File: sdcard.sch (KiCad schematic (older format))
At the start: 7 parts, among them J21 Micro_SD_Card_Det_Hirose_DM3AT

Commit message: Some small adjustments
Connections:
- net SS_SD renamed SS
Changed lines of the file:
@@
 $Descr A4 11693 8268
 encoding utf-8
-Sheet 12 12
+Sheet 11 12
 Title ""
 Date ""
@@
 SCK
 Text HLabel 3450 2850 0    50   Input ~ 0
-SS_SD
+SS
 $Comp
 L Device:R R?

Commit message: Complete functional design
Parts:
- renumbered C114 to C109, J21 to J10, R120 to R112, R121 to R113, R122 to R114, R123 to R115, R124 to R116
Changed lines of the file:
@@
 $EndDescr
 $Comp
-L Connector:Micro_SD_Card_Det_Hirose_DM3AT J21
+L Connector:Micro_SD_Card_Det_Hirose_DM3AT J10
 U 1 1 5BC78F11
 P 6000 3150
-F 0 "J21" H 5950 3967 50  0000 C CNN
+F 0 "J10" H 5950 3967 50  0000 C CNN
 F 1 "Micro_SD_Card_Det_Hirose_DM3AT" H 5950 3876 50  0000 C CNN
 F 2 "Connector_Card:microSD_HC_Hirose_DM3D-SF" H 8050 3850 50  0001 C CNN
@@
 AR Path="/5BC77F8A/5BC83407" Ref="R?"  Part="1"
 AR Path="/5BC77F8D/5BC83407" Ref="R?"  Part="1"
-AR Path="/5BC78E83/5BC83407" Ref="R124"  Part="1"
-F 0 "R124" H 4700 2450 50  0000 C CNN
+AR Path="/5BC78E83/5BC83407" Ref="R116"  Part="1"
+F 0 "R116" H 4700 2450 50  0000 C CNN
 F 1 "47k" H 4700 2550 50  0000 C CNN
 F 2 "Resistor_SMD:R_0603_1608Metric" V 4780 2500 50  0001 C CNN
@@
 SD_DETECT
 $Comp
-L power:GND #PWR0124
+L power:GND #PWR0108
 U 1 1 5BC834C8
 P 3450 3250
-F 0 "#PWR0124" H 3450 3000 50  0001 C CNN
+F 0 "#PWR0108" H 3450 3000 50  0001 C CNN
 F 1 "GND" V 3455 3122 50  0000 R CNN
 F 2 "" H 3450 3250 50  0001 C CNN
@@
 AR Path="/5BC77F8A/5BC8393A" Ref="R?"  Part="1"
 AR Path="/5BC77F8D/5BC8393A" Ref="R?"  Part="1"
-AR Path="/5BC78E83/5BC8393A" Ref="R123"  Part="1"
-F 0 "R123" H 4400 2450 50  0000 C CNN
+AR Path="/5BC78E83/5BC8393A" Ref="R115"  Part="1"
+F 0 "R115" H 4400 2450 50  0000 C CNN
 F 1 "47k" H 4400 2550 50  0000 C CNN
 F 2 "Resistor_SMD:R_0603_1608Metric" V 4480 2500 50  0001 C CNN
@@
 AR Path="/5BC77F8A/5BC842EF" Ref="R?"  Part="1"
 AR Path="/5BC77F8D/5BC842EF" Ref="R?"  Part="1"
-AR Path="/5BC78E83/5BC842EF" Ref="R122"  Part="1"
-F 0 "R122" H 4100 2450 50  0000 C CNN
+AR Path="/5BC78E83/5BC842EF" Ref="R114"  Part="1"
+F 0 "R114" H 4100 2450 50  0000 C CNN
 F 1 "47k" H 4100 2550 50  0000 C CNN
 F 2 "Resistor_SMD:R_0603_1608Metric" V 4180 2500 50  0001 C CNN
@@
 AR Path="/5BC77F8A/5BC84424" Ref="R?"  Part="1"
 AR Path="/5BC77F8D/5BC84424" Ref="R?"  Part="1"
-AR Path="/5BC78E83/5BC84424" Ref="R121"  Part="1"
-F 0 "R121" H 3800 2450 50  0000 C CNN
+AR Path="/5BC78E83/5BC84424" Ref="R113"  Part="1"
+F 0 "R113" H 3800 2450 50  0000 C CNN
 F 1 "47k" H 3800 2550 50  0000 C CNN
 F 2 "Resistor_SMD:R_0603_1608Metric" V 3880 2500 50  0001 C CNN
@@
 AR Path="/5BC77F8A/5BC8859F" Ref="R?"  Part="1"
 AR Path="/5BC77F8D/5BC8859F" Ref="R?"  Part="1"
-AR Path="/5BC78E83/5BC8859F" Ref="R120"  Part="1"
-F 0 "R120" H 3500 2450 50  0000 C CNN
+AR Path="/5BC78E83/5BC8859F" Ref="R112"  Part="1"
+F 0 "R112" H 3500 2450 50  0000 C CNN
 F 1 "47k" H 3500 2550 50  0000 C CNN
 F 2 "Resistor_SMD:R_0603_1608Metric" V 3580 2500 50  0001 C CNN
@@
 	3650 3450 5100 3450
 $Comp
-L power:GND #PWR0126
+L power:GND #PWR0110
 U 1 1 5BC89EBA
 P 6800 3650
-F 0 "#PWR0126" H 6800 3400 50  0001 C CNN
+F 0 "#PWR0110" H 6800 3400 50  0001 C CNN
 F 1 "GND" H 6805 3477 50  0000 C CNN
 F 2 "" H 6800 3650 50  0001 C CNN
@@
 P 4400 3850
 AR Path="/5BC54251/5BC90131" Ref="C?"  Part="1"
-AR Path="/5BC78E83/5BC90131" Ref="C114"  Part="1"
-F 0 "C114" H 4515 3896 50  0000 L CNN
+AR Path="/5BC78E83/5BC90131" Ref="C109"  Part="1"
+F 0 "C109" H 4515 3896 50  0000 L CNN
 F 1 "10uF" H 4515 3805 50  0000 L CNN
 F 2 "Capacitor_SMD:C_1206_3216Metric" H 4438 3700 50  0001 C CNN
@@
 VDD3V3
 $Comp
-L power:GND #PWR0125
+L power:GND #PWR0109
 U 1 1 5BC911BE
 P 4400 4000
-F 0 "#PWR0125" H 4400 3750 50  0001 C CNN
+F 0 "#PWR0109" H 4400 3750 50  0001 C CNN
 F 1 "GND" H 4405 3827 50  0000 C CNN
 F 2 "" H 4400 4000 50  0001 C CNN

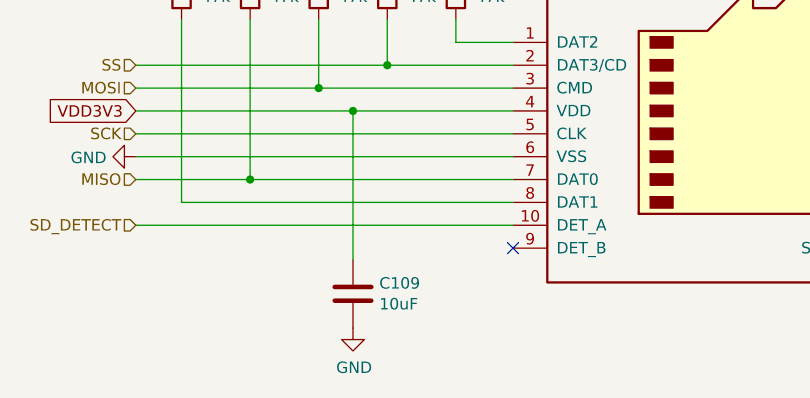
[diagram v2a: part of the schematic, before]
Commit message: Add bypass cap for I2C EEPROMs and redone some copper pour
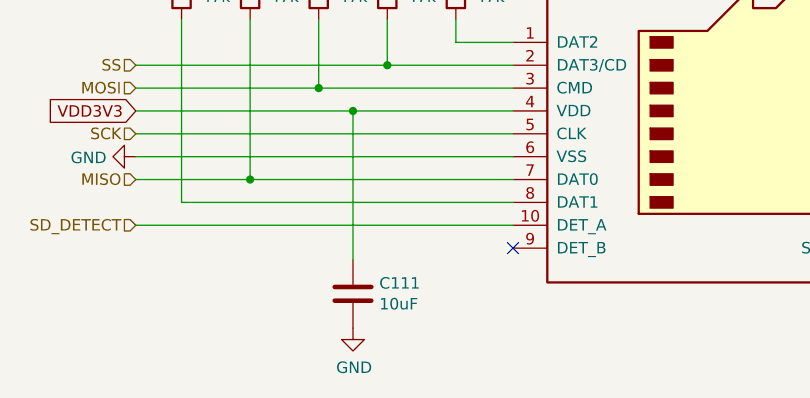
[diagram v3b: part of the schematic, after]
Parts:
- renumbered C109 to C111
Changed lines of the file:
@@
 SD_DETECT
 $Comp
-L power:GND #PWR0108
+L power:GND #PWR0110
 U 1 1 5BC834C8
 P 3450 3250
-F 0 "#PWR0108" H 3450 3000 50  0001 C CNN
+F 0 "#PWR0110" H 3450 3000 50  0001 C CNN
 F 1 "GND" V 3455 3122 50  0000 R CNN
 F 2 "" H 3450 3250 50  0001 C CNN
@@
 	3650 3450 5100 3450
 $Comp
-L power:GND #PWR0110
+L power:GND #PWR0112
 U 1 1 5BC89EBA
 P 6800 3650
-F 0 "#PWR0110" H 6800 3400 50  0001 C CNN
+F 0 "#PWR0112" H 6800 3400 50  0001 C CNN
 F 1 "GND" H 6805 3477 50  0000 C CNN
 F 2 "" H 6800 3650 50  0001 C CNN
@@
 P 4400 3850
 AR Path="/5BC54251/5BC90131" Ref="C?"  Part="1"
-AR Path="/5BC78E83/5BC90131" Ref="C109"  Part="1"
-F 0 "C109" H 4515 3896 50  0000 L CNN
+AR Path="/5BC78E83/5BC90131" Ref="C111"  Part="1"
+F 0 "C111" H 4515 3896 50  0000 L CNN
 F 1 "10uF" H 4515 3805 50  0000 L CNN
 F 2 "Capacitor_SMD:C_1206_3216Metric" H 4438 3700 50  0001 C CNN
@@
 VDD3V3
 $Comp
-L power:GND #PWR0109
+L power:GND #PWR0111
 U 1 1 5BC911BE
 P 4400 4000
-F 0 "#PWR0109" H 4400 3750 50  0001 C CNN
+F 0 "#PWR0111" H 4400 3750 50  0001 C CNN
 F 1 "GND" H 4405 3827 50  0000 C CNN
 F 2 "" H 4400 4000 50  0001 C CNN

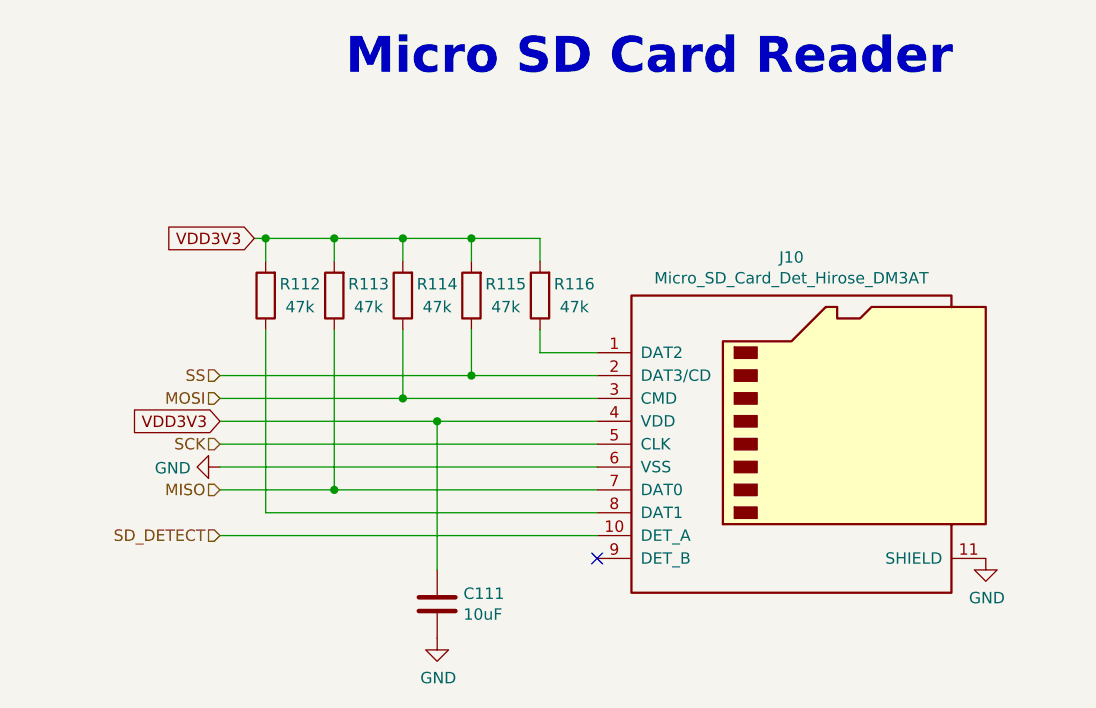
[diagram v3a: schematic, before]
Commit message: Add transistor for boot selection
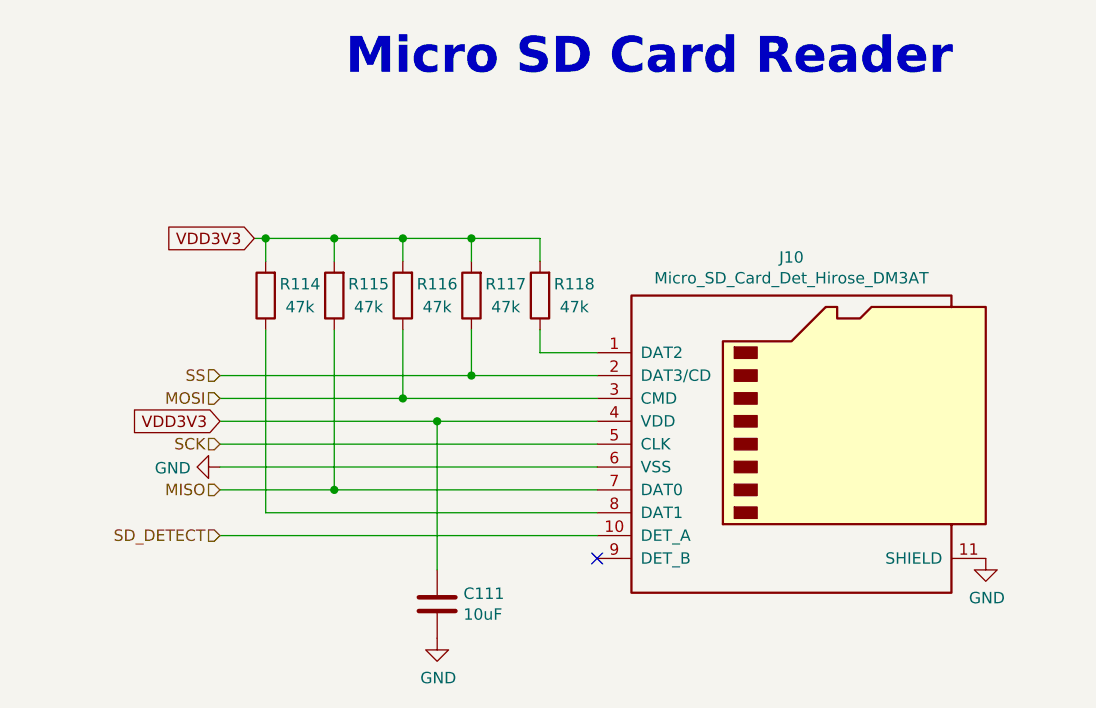
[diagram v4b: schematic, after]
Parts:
- renumbered R112 to R114, R113 to R115, R114 to R116, R115 to R117, R116 to R118
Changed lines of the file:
@@
 AR Path="/5BC77F8A/5BC83407" Ref="R?"  Part="1"
 AR Path="/5BC77F8D/5BC83407" Ref="R?"  Part="1"
-AR Path="/5BC78E83/5BC83407" Ref="R116"  Part="1"
-F 0 "R116" H 4700 2450 50  0000 C CNN
+AR Path="/5BC78E83/5BC83407" Ref="R118"  Part="1"
+F 0 "R118" H 4700 2450 50  0000 C CNN
 F 1 "47k" H 4700 2550 50  0000 C CNN
 F 2 "Resistor_SMD:R_0603_1608Metric" V 4780 2500 50  0001 C CNN
@@
 AR Path="/5BC77F8A/5BC8393A" Ref="R?"  Part="1"
 AR Path="/5BC77F8D/5BC8393A" Ref="R?"  Part="1"
-AR Path="/5BC78E83/5BC8393A" Ref="R115"  Part="1"
-F 0 "R115" H 4400 2450 50  0000 C CNN
+AR Path="/5BC78E83/5BC8393A" Ref="R117"  Part="1"
+F 0 "R117" H 4400 2450 50  0000 C CNN
 F 1 "47k" H 4400 2550 50  0000 C CNN
 F 2 "Resistor_SMD:R_0603_1608Metric" V 4480 2500 50  0001 C CNN
@@
 AR Path="/5BC77F8A/5BC842EF" Ref="R?"  Part="1"
 AR Path="/5BC77F8D/5BC842EF" Ref="R?"  Part="1"
-AR Path="/5BC78E83/5BC842EF" Ref="R114"  Part="1"
-F 0 "R114" H 4100 2450 50  0000 C CNN
+AR Path="/5BC78E83/5BC842EF" Ref="R116"  Part="1"
+F 0 "R116" H 4100 2450 50  0000 C CNN
 F 1 "47k" H 4100 2550 50  0000 C CNN
 F 2 "Resistor_SMD:R_0603_1608Metric" V 4180 2500 50  0001 C CNN
@@
 AR Path="/5BC77F8A/5BC84424" Ref="R?"  Part="1"
 AR Path="/5BC77F8D/5BC84424" Ref="R?"  Part="1"
-AR Path="/5BC78E83/5BC84424" Ref="R113"  Part="1"
-F 0 "R113" H 3800 2450 50  0000 C CNN
+AR Path="/5BC78E83/5BC84424" Ref="R115"  Part="1"
+F 0 "R115" H 3800 2450 50  0000 C CNN
 F 1 "47k" H 3800 2550 50  0000 C CNN
 F 2 "Resistor_SMD:R_0603_1608Metric" V 3880 2500 50  0001 C CNN
@@
 AR Path="/5BC77F8A/5BC8859F" Ref="R?"  Part="1"
 AR Path="/5BC77F8D/5BC8859F" Ref="R?"  Part="1"
-AR Path="/5BC78E83/5BC8859F" Ref="R112"  Part="1"
-F 0 "R112" H 3500 2450 50  0000 C CNN
+AR Path="/5BC78E83/5BC8859F" Ref="R114"  Part="1"
+F 0 "R114" H 3500 2450 50  0000 C CNN
 F 1 "47k" H 3500 2550 50  0000 C CNN
 F 2 "Resistor_SMD:R_0603_1608Metric" V 3580 2500 50  0001 C CNN

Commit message: Correct the name of the micro SD card reader
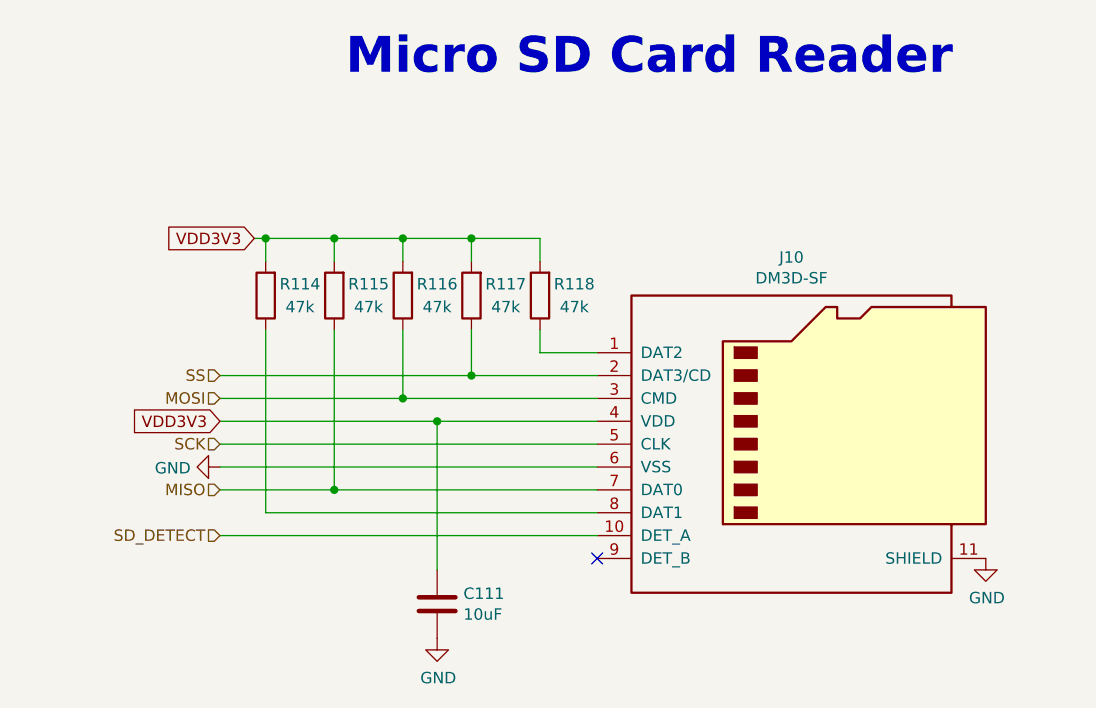
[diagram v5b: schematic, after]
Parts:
- J10: value Micro_SD_Card_Det_Hirose_DM3AT -> DM3D-SF
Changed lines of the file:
@@
 P 6000 3150
 F 0 "J10" H 5950 3967 50  0000 C CNN
-F 1 "Micro_SD_Card_Det_Hirose_DM3AT" H 5950 3876 50  0000 C CNN
+F 1 "DM3D-SF" H 5950 3876 50  0000 C CNN
 F 2 "Connector_Card:microSD_HC_Hirose_DM3D-SF" H 8050 3850 50  0001 C CNN
 F 3 "https://www.hirose.com/product/en/download_file/key_name/DM3/category/Catalog/doc_file_id/49662/?file_category_id=4&item_id=195&is_series=1" H 6000 3250 50  0001 C CNN

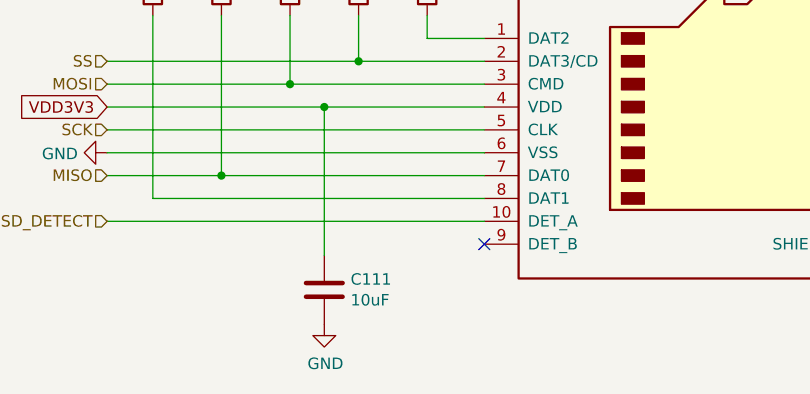
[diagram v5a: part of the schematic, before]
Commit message: Fix various v1.0 errors
 * Change 3.3V LDO to AP7365-33WG-7
 * Optimize soldermask clearance (from 0.2 to 0.05)
 * Connect SD connect switch to GND
 * Optimized some PADs
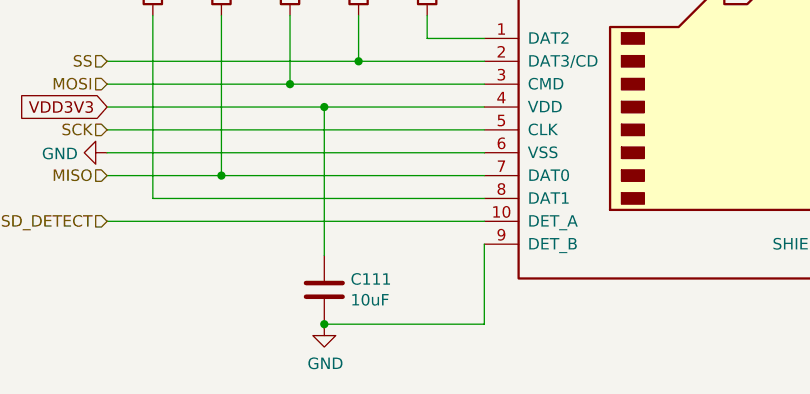
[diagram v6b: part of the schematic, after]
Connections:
- net GND: now also J10.9 (DET_B)
- no-connect marks 1 -> 0
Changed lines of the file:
@@
 Wire Wire Line
 	4850 2750 5100 2750
-NoConn ~ 5100 3650
 Text GLabel 3600 2250 0    50   Input ~ 0
 VDD3V3
@@
 	1    0    0    -1
 $EndComp
+Wire Wire Line
+	5100 4000 4400 4000
+Wire Wire Line
+	5100 3650 5100 4000
+Connection ~ 4400 4000
 $EndSCHEMATC
